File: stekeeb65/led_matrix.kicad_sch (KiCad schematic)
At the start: 66 parts

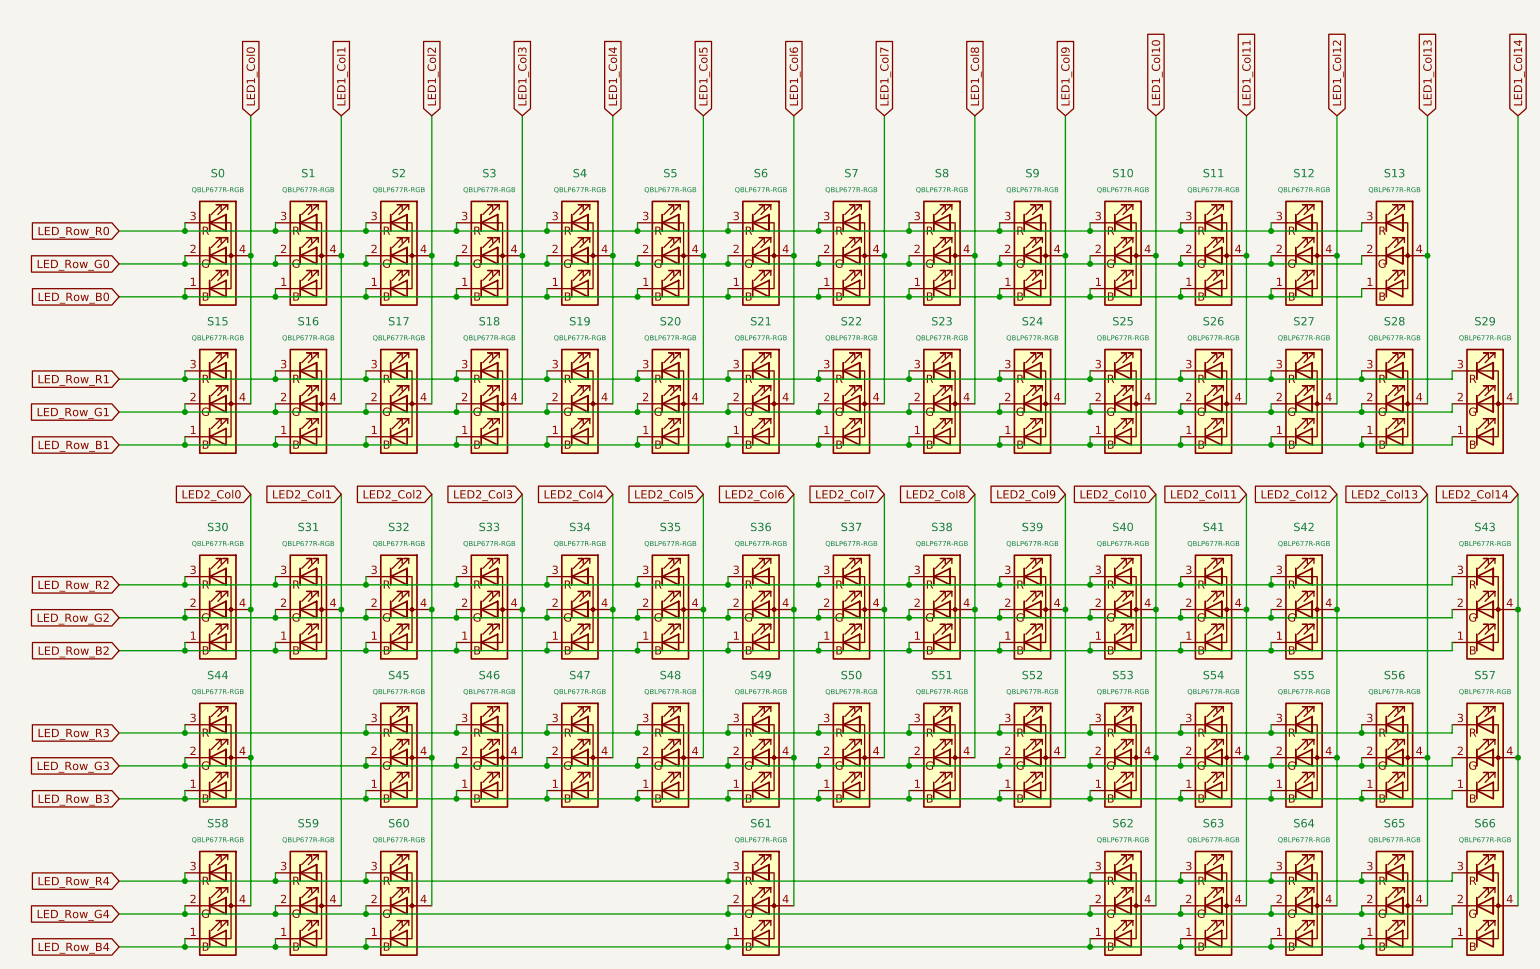
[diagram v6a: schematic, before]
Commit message: Finish routing matrix
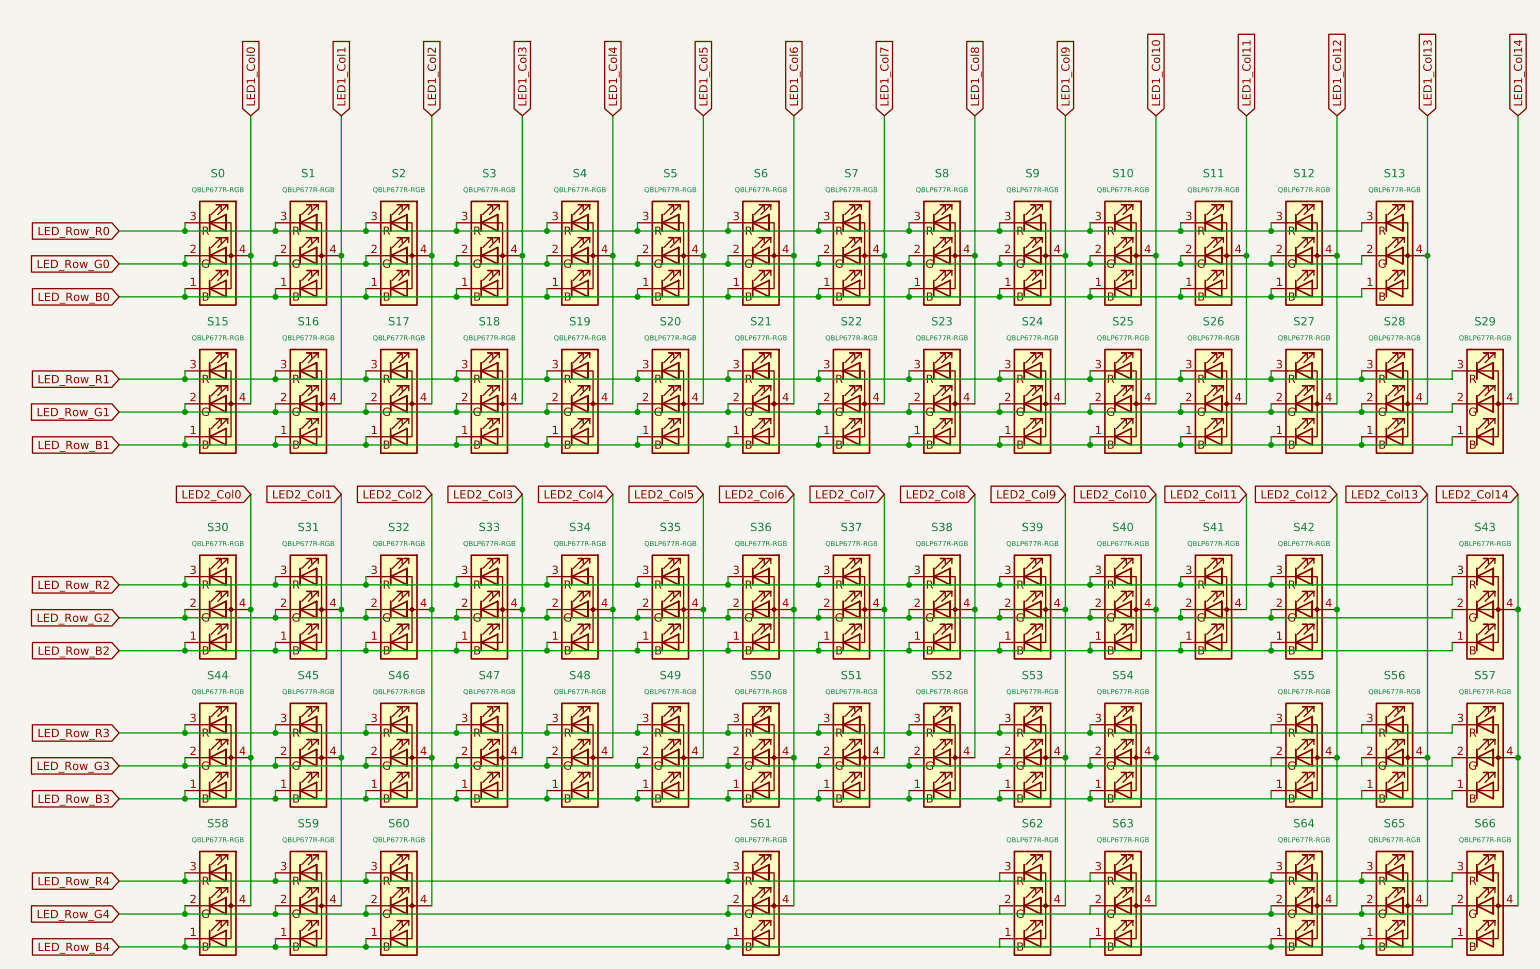
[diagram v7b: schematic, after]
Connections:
- net LED2_Col1: now also S45.4 (A)
- net LED2_Col10: now also S54.4 (A), S63.4 (A); no longer S53.4 (A), S62.4 (A)
- net LED2_Col11: no longer S54.4 (A), S63.4 (A)
- net LED2_Col2: now also S46.4 (A); no longer S45.4 (A)
- net LED2_Col3: now also S47.4 (A); no longer S46.4 (A)
- net LED2_Col4: now also S48.4 (A); no longer S47.4 (A)
- net LED2_Col5: now also S49.4 (A); no longer S48.4 (A)
- net LED2_Col6: now also S50.4 (A); no longer S49.4 (A)
- net LED2_Col7: now also S51.4 (A); no longer S50.4 (A)
- net LED2_Col8: now also S52.4 (A); no longer S51.4 (A)
- net LED2_Col9: now also S53.4 (A), S62.4 (A); no longer S52.4 (A)
- net LED_Row_B3: no longer S55.1 (BK), S56.1 (BK)
- net LED_Row_B4: no longer S62.1 (BK), S63.1 (BK)
- net LED_Row_G3: no longer S55.2 (GK), S56.2 (GK)
- net LED_Row_G4: no longer S62.2 (GK), S63.2 (GK)
- net LED_Row_R3: no longer S55.3 (RK), S56.3 (RK)
- net LED_Row_R4: no longer S62.3 (RK), S63.3 (RK)
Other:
- moved on the sheet: S45, S46, S47, S48, S49, S50, S51, S52, S53, S54, S62, S63

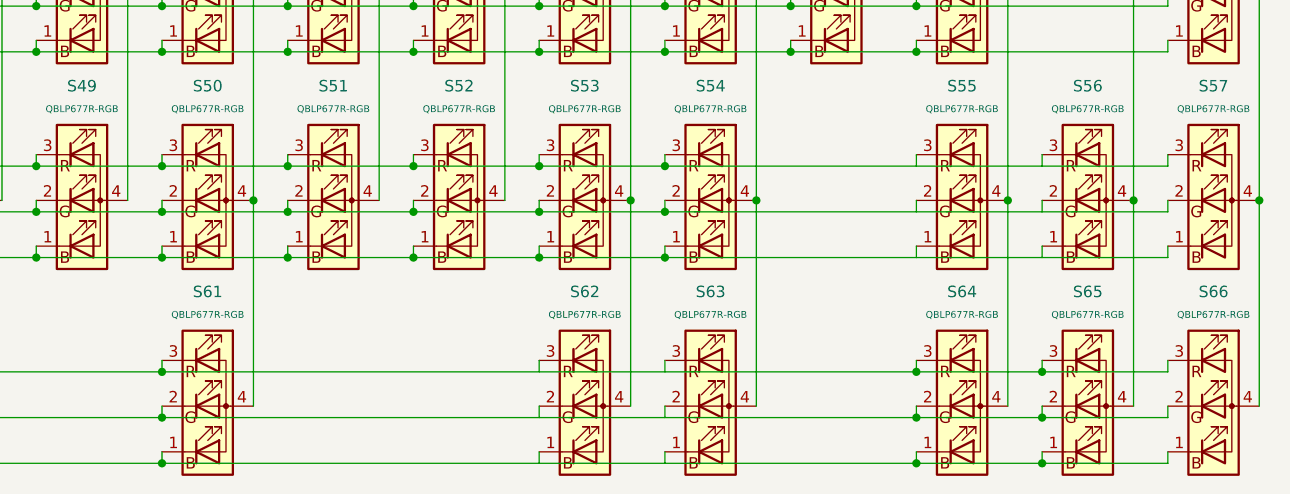
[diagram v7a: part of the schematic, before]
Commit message: Replacing Type-C in lieu of a daughter board connector.
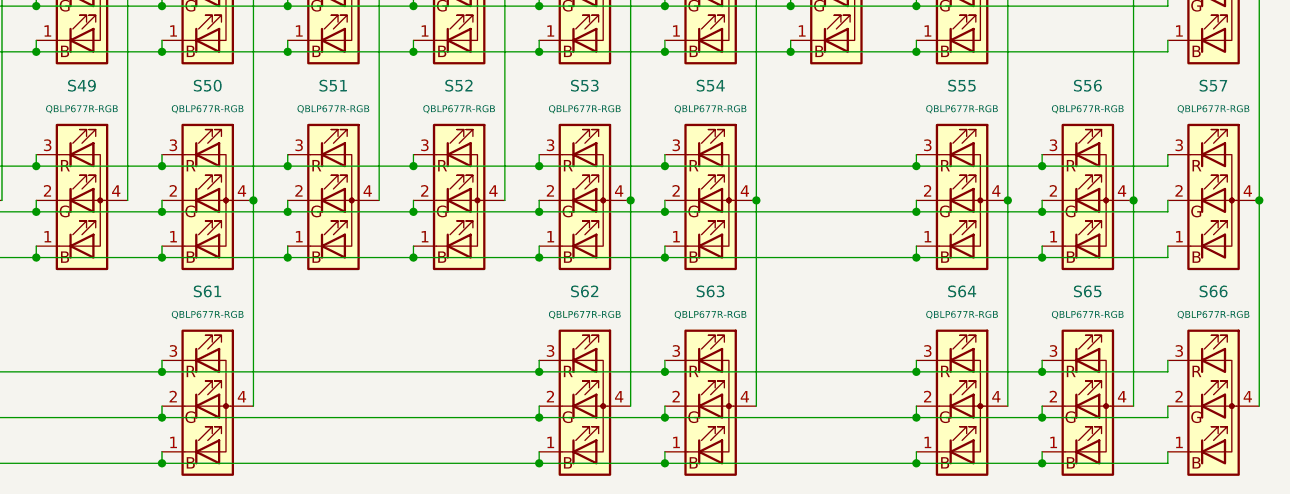
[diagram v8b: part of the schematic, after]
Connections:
- net LED_Row_B3: now also S55.1 (BK), S56.1 (BK)
- net LED_Row_B4: now also S62.1 (BK), S63.1 (BK)
- net LED_Row_G3: now also S55.2 (GK), S56.2 (GK)
- net LED_Row_G4: now also S62.2 (GK), S63.2 (GK)
- net LED_Row_R3: now also S55.3 (RK), S56.3 (RK)
- net LED_Row_R4: now also S62.3 (RK), S63.3 (RK)
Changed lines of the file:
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@@
   (junction (at 148.59 128.27) (diameter 0) (color 0 0 0 0)
   )
+  (junction (at 176.53 151.13) (diameter 0) (color 0 0 0 0)
+  )
   (junction (at 74.93 49.53) (diameter 0) (color 0 0 0 0)
   )
   (junction (at 88.9 127) (diameter 0) (color 0 0 0 0)
   )
+  (junction (at 232.41 128.27) (diameter 0) (color 0 0 0 0)
+  )
   (junction (at 176.53 110.49) (diameter 0) (color 0 0 0 0)
   )
+  (junction (at 232.41 123.19) (diameter 0) (color 0 0 0 0)
+  )
   (junction (at 134.62 151.13) (diameter 0) (color 0 0 0 0)
   )
@@
   (junction (at 232.41 78.74) (diameter 0) (color 0 0 0 0)
   )
+  (junction (at 176.53 146.05) (diameter 0) (color 0 0 0 0)
+  )
   (junction (at 60.96 127) (diameter 0) (color 0 0 0 0)
   )
@@
   (junction (at 78.74 68.58) (diameter 0) (color 0 0 0 0)
   )
+  (junction (at 190.5 146.05) (diameter 0) (color 0 0 0 0)
+  )
   (junction (at 218.44 110.49) (diameter 0) (color 0 0 0 0)
   )
@@
   (junction (at 200.66 49.53) (diameter 0) (color 0 0 0 0)
   )
+  (junction (at 218.44 123.19) (diameter 0) (color 0 0 0 0)
+  )
   (junction (at 106.68 45.72) (diameter 0) (color 0 0 0 0)
   )
@@
   (junction (at 144.78 127) (diameter 0) (color 0 0 0 0)
   )
+  (junction (at 190.5 156.21) (diameter 0) (color 0 0 0 0)
+  )
   (junction (at 64.77 156.21) (diameter 0) (color 0 0 0 0)
   )
@@
   (junction (at 176.53 123.19) (diameter 0) (color 0 0 0 0)
   )
+  (junction (at 176.53 156.21) (diameter 0) (color 0 0 0 0)
+  )
   (junction (at 64.77 146.05) (diameter 0) (color 0 0 0 0)
   )
@@
   (junction (at 106.68 68.58) (diameter 0) (color 0 0 0 0)
   )
+  (junction (at 218.44 128.27) (diameter 0) (color 0 0 0 0)
+  )
   (junction (at 176.53 78.74) (diameter 0) (color 0 0 0 0)
   )
@@
   (junction (at 204.47 73.66) (diameter 0) (color 0 0 0 0)
   )
+  (junction (at 218.44 133.35) (diameter 0) (color 0 0 0 0)
+  )
   (junction (at 64.77 45.72) (diameter 0) (color 0 0 0 0)
   )
@@
   (junction (at 218.44 78.74) (diameter 0) (color 0 0 0 0)
   )
+  (junction (at 232.41 133.35) (diameter 0) (color 0 0 0 0)
+  )
   (junction (at 148.59 133.35) (diameter 0) (color 0 0 0 0)
   )
@@
   (junction (at 50.8 50.8) (diameter 0) (color 0 0 0 0)
   )
+  (junction (at 190.5 151.13) (diameter 0) (color 0 0 0 0)
+  )
   (junction (at 50.8 110.49) (diameter 0) (color 0 0 0 0)
   )
@@
     (stroke (width 0) (type default) (color 0 0 0 0))
   )
+  (wire (pts (xy 190.5 146.05) (xy 218.44 146.05))
+    (stroke (width 0) (type default) (color 0 0 0 0))
+  )
   (wire (pts (xy 218.44 55.88) (xy 232.41 55.88))
     (stroke (width 0) (type default) (color 0 0 0 0))
@@
     (stroke (width 0) (type default) (color 0 0 0 0))
   )
-  (wire (pts (xy 190.5 133.35) (xy 246.38 133.35))
+  (wire (pts (xy 190.5 133.35) (xy 218.44 133.35))
     (stroke (width 0) (type default) (color 0 0 0 0))
   )
@@
     (stroke (width 0) (type default) (color 0 0 0 0))
   )
+  (wire (pts (xy 176.53 151.13) (xy 190.5 151.13))
+    (stroke (width 0) (type default) (color 0 0 0 0))
+  )
   (wire (pts (xy 144.78 27.94) (xy 144.78 49.53))
     (stroke (width 0) (type default) (color 0 0 0 0))
@@
     (stroke (width 0) (type default) (color 0 0 0 0))
   )
+  (wire (pts (xy 190.5 156.21) (xy 218.44 156.21))
+    (stroke (width 0) (type default) (color 0 0 0 0))
+  )
   (wire (pts (xy 92.71 73.66) (xy 92.71 72.39))
     (stroke (width 0) (type default) (color 0 0 0 0))
@@
     (stroke (width 0) (type default) (color 0 0 0 0))
   )
+  (wire (pts (xy 190.5 151.13) (xy 218.44 151.13))
+    (stroke (width 0) (type default) (color 0 0 0 0))
+  )
   (wire (pts (xy 134.62 133.35) (xy 148.59 133.35))
     (stroke (width 0) (type default) (color 0 0 0 0))
@@
     (stroke (width 0) (type default) (color 0 0 0 0))
   )
+  (wire (pts (xy 218.44 128.27) (xy 232.41 128.27))
+    (stroke (width 0) (type default) (color 0 0 0 0))
+  )
   (wire (pts (xy 190.5 45.72) (xy 204.47 45.72))
     (stroke (width 0) (type default) (color 0 0 0 0))
@@
     (stroke (width 0) (type default) (color 0 0 0 0))
   )
+  (wire (pts (xy 134.62 146.05) (xy 176.53 146.05))
+    (stroke (width 0) (type default) (color 0 0 0 0))
+  )
   (wire (pts (xy 40.64 105.41) (xy 50.8 105.41))
     (stroke (width 0) (type default) (color 0 0 0 0))
@@
     (stroke (width 0) (type default) (color 0 0 0 0))
   )
+  (wire (pts (xy 232.41 123.19) (xy 246.38 123.19))
+    (stroke (width 0) (type default) (color 0 0 0 0))
+  )
   (wire (pts (xy 190.5 110.49) (xy 204.47 110.49))
     (stroke (width 0) (type default) (color 0 0 0 0))
@@
     (stroke (width 0) (type default) (color 0 0 0 0))
   )
-  (wire (pts (xy 134.62 146.05) (xy 218.44 146.05))
-    (stroke (width 0) (type default) (color 0 0 0 0))
-  )
   (wire (pts (xy 74.93 104.14) (xy 74.93 127))
     (stroke (width 0) (type default) (color 0 0 0 0))
@@
     (stroke (width 0) (type default) (color 0 0 0 0))
   )
+  (wire (pts (xy 232.41 128.27) (xy 246.38 128.27))
+    (stroke (width 0) (type default) (color 0 0 0 0))
+  )
   (wire (pts (xy 148.59 133.35) (xy 162.56 133.35))
     (stroke (width 0) (type default) (color 0 0 0 0))
@@
     (stroke (width 0) (type default) (color 0 0 0 0))
   )
+  (wire (pts (xy 176.53 146.05) (xy 190.5 146.05))
+    (stroke (width 0) (type default) (color 0 0 0 0))
+  )
   (wire (pts (xy 120.65 100.33) (xy 120.65 99.06))
     (stroke (width 0) (type default) (color 0 0 0 0))
@@
     (stroke (width 0) (type default) (color 0 0 0 0))
   )
-  (wire (pts (xy 190.5 128.27) (xy 246.38 128.27))
+  (wire (pts (xy 190.5 128.27) (xy 218.44 128.27))
     (stroke (width 0) (type default) (color 0 0 0 0))
   )
@@
     (stroke (width 0) (type default) (color 0 0 0 0))
   )
-  (wire (pts (xy 134.62 156.21) (xy 218.44 156.21))
+  (wire (pts (xy 134.62 156.21) (xy 176.53 156.21))
     (stroke (width 0) (type default) (color 0 0 0 0))
   )
@@
     (stroke (width 0) (type default) (color 0 0 0 0))
   )
+  (wire (pts (xy 232.41 133.35) (xy 246.38 133.35))
+    (stroke (width 0) (type default) (color 0 0 0 0))
+  )
   (wire (pts (xy 162.56 128.27) (xy 176.53 128.27))
     (stroke (width 0) (type default) (color 0 0 0 0))
@@
     (stroke (width 0) (type default) (color 0 0 0 0))
   )
-  (wire (pts (xy 134.62 151.13) (xy 218.44 151.13))
+  (wire (pts (xy 134.62 151.13) (xy 176.53 151.13))
     (stroke (width 0) (type default) (color 0 0 0 0))
   )
@@
     (stroke (width 0) (type default) (color 0 0 0 0))
   )
-  (wire (pts (xy 190.5 123.19) (xy 246.38 123.19))
+  (wire (pts (xy 190.5 123.19) (xy 218.44 123.19))
     (stroke (width 0) (type default) (color 0 0 0 0))
   )
@@
     (stroke (width 0) (type default) (color 0 0 0 0))
   )
+  (wire (pts (xy 218.44 133.35) (xy 232.41 133.35))
+    (stroke (width 0) (type default) (color 0 0 0 0))
+  )
   (wire (pts (xy 120.65 133.35) (xy 120.65 132.08))
     (stroke (width 0) (type default) (color 0 0 0 0))
@@
     (stroke (width 0) (type default) (color 0 0 0 0))
   )
+  (wire (pts (xy 218.44 123.19) (xy 232.41 123.19))
+    (stroke (width 0) (type default) (color 0 0 0 0))
+  )
   (wire (pts (xy 74.93 27.94) (xy 74.93 49.53))
     (stroke (width 0) (type default) (color 0 0 0 0))
@@
     (stroke (width 0) (type default) (color 0 0 0 0))
   )
+  (wire (pts (xy 176.53 156.21) (xy 190.5 156.21))
+    (stroke (width 0) (type default) (color 0 0 0 0))
+  )
